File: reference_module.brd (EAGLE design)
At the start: 160 x 100 mm, 96 parts, among them IC1 LM324N, IC2 LM741P, IC3 LM741P, IC4 7812T, IC5 7812T

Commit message: Board file
Component placing done.
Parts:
- added C16, C17: 0.1UF/100V, amit_rcl:C102-054X133
- C11, C15: value 1UF/63V -> 0.1UF/100V; device amit_rcl:E3,5-10 -> amit_rcl:C102-054X133
- moved F1 462.7 mm to (173.0, 20.0)
- moved ZD1 422.1 mm to (124.0, 102.0), turned to 90 degrees
- moved ZD2 420.8 mm to (119.0, 102.0), turned to 270 degrees
- moved ZD4 380.8 mm to (80.0, 75.0), turned to 270 degrees
- moved C15 375.8 mm to (25.0, 91.0)
- moved ZD3 373.7 mm to (77.0, 75.0), turned to 270 degrees
- moved IC2 367.4 mm to (44.0, 50.0)
- moved ZD6 361.2 mm to (42.0, 75.0), turned to 270 degrees
- moved C11 357.1 mm to (26.0, 75.0), turned to 90 degrees
- moved IC3 353.1 mm to (12.0, 50.0)
- moved ZD5 353.0 mm to (38.0, 75.0), turned to 270 degrees
- moved D17 352.7 mm to (116.0, 22.0), turned to 270 degrees
- moved D18 348.3 mm to (113.0, 22.0), turned to 270 degrees
- moved S1 333.9 mm to (83.0, 101.0)
- moved IC1 322.3 mm to (90.0, 53.0)
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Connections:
- removed net N$56: D28.A, RV8.E, S1.14, S1.15, S1.16
- new net N$68: C16.2, D28.A, RV8.E, S1.1, S1.2, S1.3
- net N$20: now also X1.14
- net N$31: now also S1.9; no longer S1.8
- net N$32: now also S1.8; no longer S1.9
- net N$38: now also S1.10; no longer S1.7
- net N$40: now also S1.11; no longer S1.6
- net N$41: now also S1.6, S1.7; no longer S1.10, S1.11
- net N$47: now also C15.2, S1.15; no longer C15.-, S1.2
- net N$48: now also C11.1, C17.1; no longer C11.+
- net N$49: now also C11.2, S1.13; no longer C11.-, S1.4
- net N$54: now also C17.2, S1.4; no longer S1.13
- net N$55: now also C15.1, C16.1, S1.16; no longer C15.+, S1.1
- net N$57: now also S1.14, S1.5; no longer S1.12, S1.3
- net N$59: now also S1.12; no longer S1.5
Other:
- board size 160 x 100 mm -> 195 x 115 mm

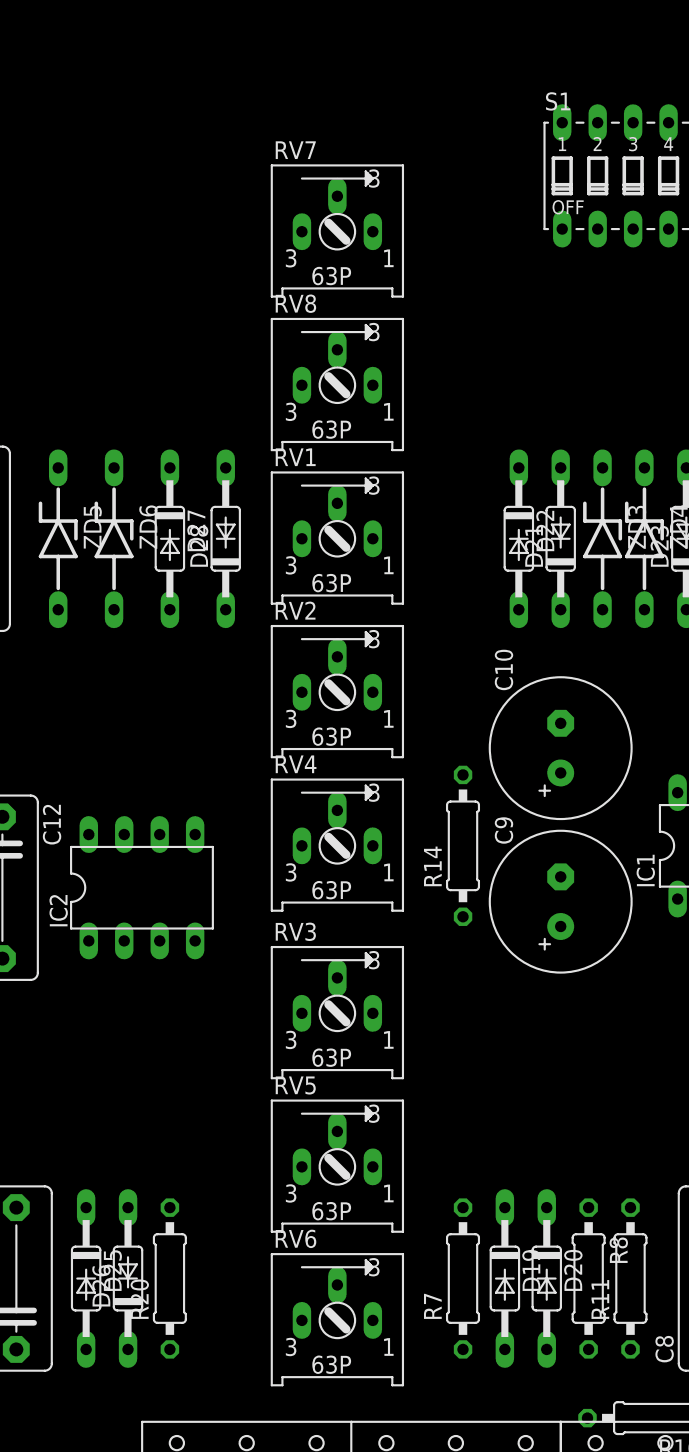
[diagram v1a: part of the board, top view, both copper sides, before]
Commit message: schematic and PCB
changed D26 connection
added +vcc and -vcc to IC
schematic verified.
PCB layout done in diptrace.
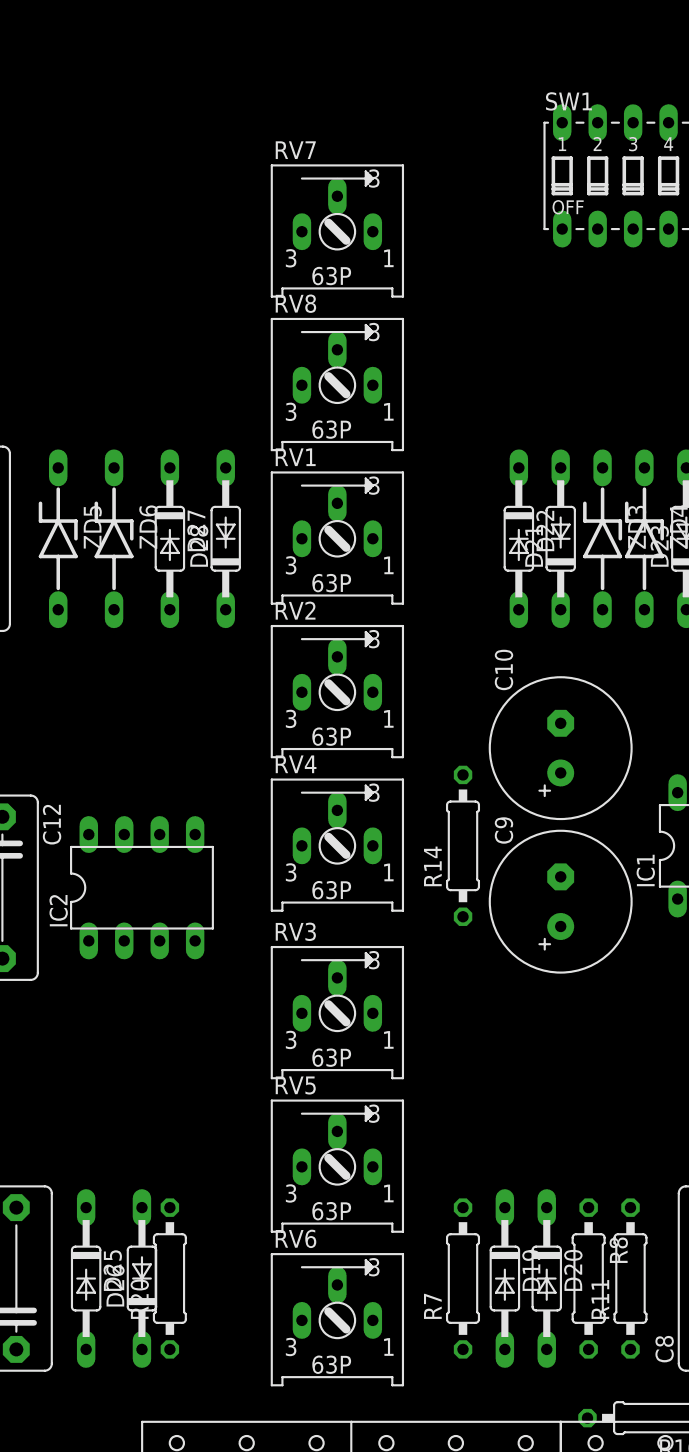
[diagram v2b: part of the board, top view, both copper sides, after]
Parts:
- moved D26 1.00 mm to (44.0, 22.0)
- renumbered S1 to SW1
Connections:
- removed net N$10: C1.-, C12.2, C13.2, C2.-, C4.+, C5.2, C6.2, C8.2, D10.C, D2.A, D23.C, D24.A, D25.A, D26.A, D4.A, D9.A, IC1.12, IC4.2, IC5.3, R20.1, RV2.E, RV4.E, RV8.A, X1.10, X1.15, X1.21, X1.3, ZD1.C
- removed net N$26: C2.+, D11.C, D13.C, D15.C, D17.C, D19.C, D21.C, D29.C, D31.C, D9.C, IC4.3, X1.19, X1.20
- removed net V+: IC1.4, IC2.7, IC3.7
- removed net V-: IC1.11, IC2.4, IC3.4
- new net +VCC: C2.+, D11.C, D13.C, D15.C, D17.C, D19.C, D21.C, D29.C, D31.C, D9.C, IC1.4, IC2.7, IC3.7, IC4.3, X1.19, X1.20
- new net -VCC: C1.-, C12.2, C13.2, C2.-, C4.+, C5.2, C6.2, C8.2, D10.C, D2.A, D23.C, D24.A, D25.A, D26.C, D4.A, D9.A, IC1.11, IC1.12, IC2.4, IC3.4, IC4.2, IC5.3, R20.1, RV2.E, RV4.E, RV8.A, X1.10, X1.15, X1.21, X1.3, ZD1.C
- net N$54: now also D26.A; no longer D26.C
